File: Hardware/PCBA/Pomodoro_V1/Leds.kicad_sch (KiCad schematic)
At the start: 0 parts

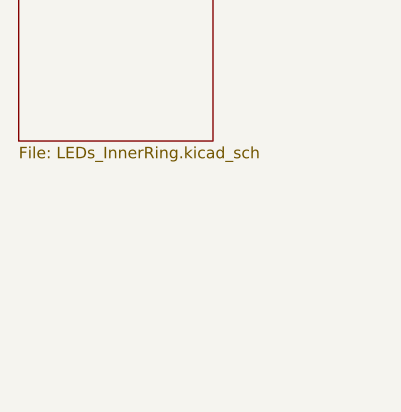
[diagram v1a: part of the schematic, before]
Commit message: Implemented the Rotary encoder, the buttons, the IMU, Added it to the PCB (All the space constraining elements are now placed)
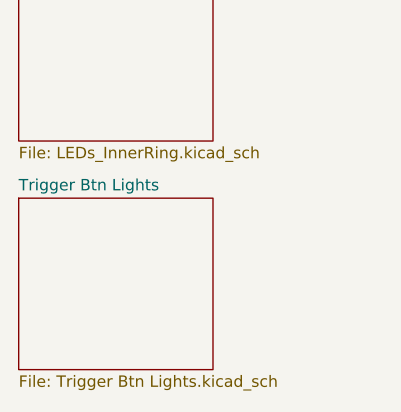
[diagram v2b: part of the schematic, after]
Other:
- added sheet Trigger Btn Lights (Trigger Btn Lights.kicad_sch)
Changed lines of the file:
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@@
+		)
+	)
+	(sheet
+		(at 52.07 125.73)
+		(size 21.59 19.05)
+		(fields_autoplaced yes)
+		(stroke
+			(width 0.1524)
+			(type solid)
+		)
+		(fill
+			(color 0 0 0 0.0000)
+		)
+		(property "Sheetname" "Trigger Btn Lights"
+			(at 52.07 125.0184 0)
+			(effects
+				(font
+					(size 1.27 1.27)
+				)
+				(justify left bottom)
+			)
+		)
+		(property "Sheetfile" "Trigger Btn Lights.kicad_sch"
+			(at 52.07 145.3646 0)
+			(effects
+				(font
+					(size 1.27 1.27)
+				)
+				(justify left top)
+			)
+		)
+		(instances
+			(project "Pomodoro_V1"
+				(path "/8b8515f0-2a7a-4fc4-bc5a-86877c499298/229321d6-581c-43f0-99a7-d20c362b1348"
+					(page "10")
+				)
+			)
 		)
 	)
